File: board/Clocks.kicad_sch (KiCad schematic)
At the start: 9 parts, among them J4 ATX-20, U36 74HC14, U37 74LS191, Y1 14.31818MHz

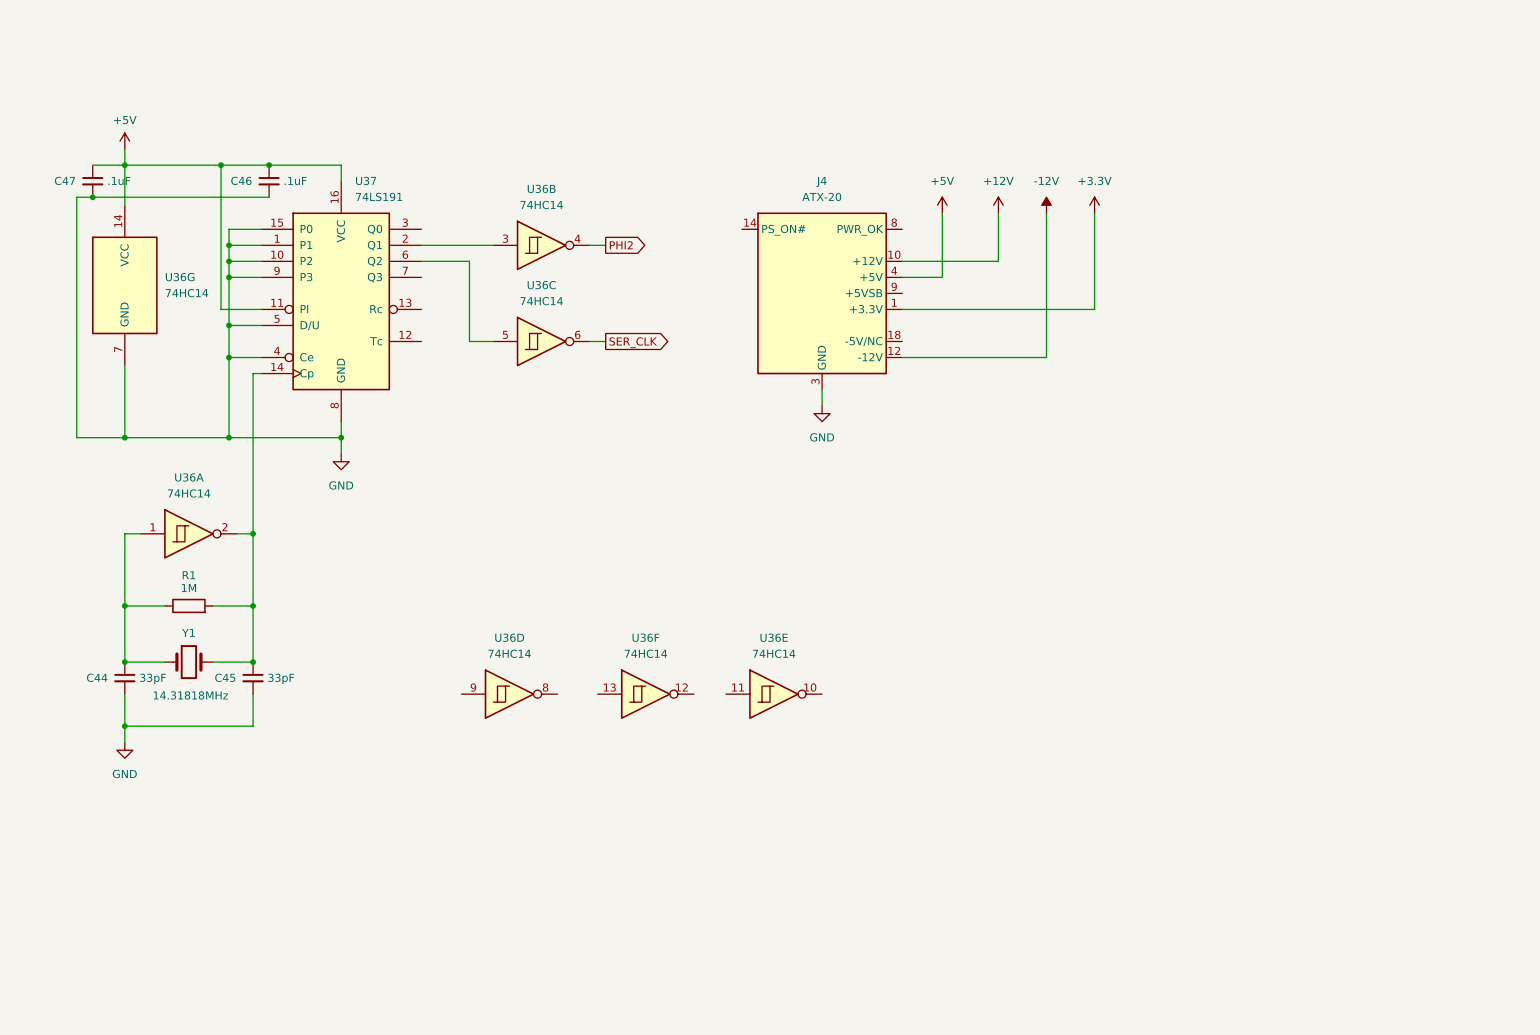
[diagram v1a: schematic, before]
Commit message: Changing to ATX-sized motherboard with 8 62-pin ISA slots.  Other component connection cleanup as well.
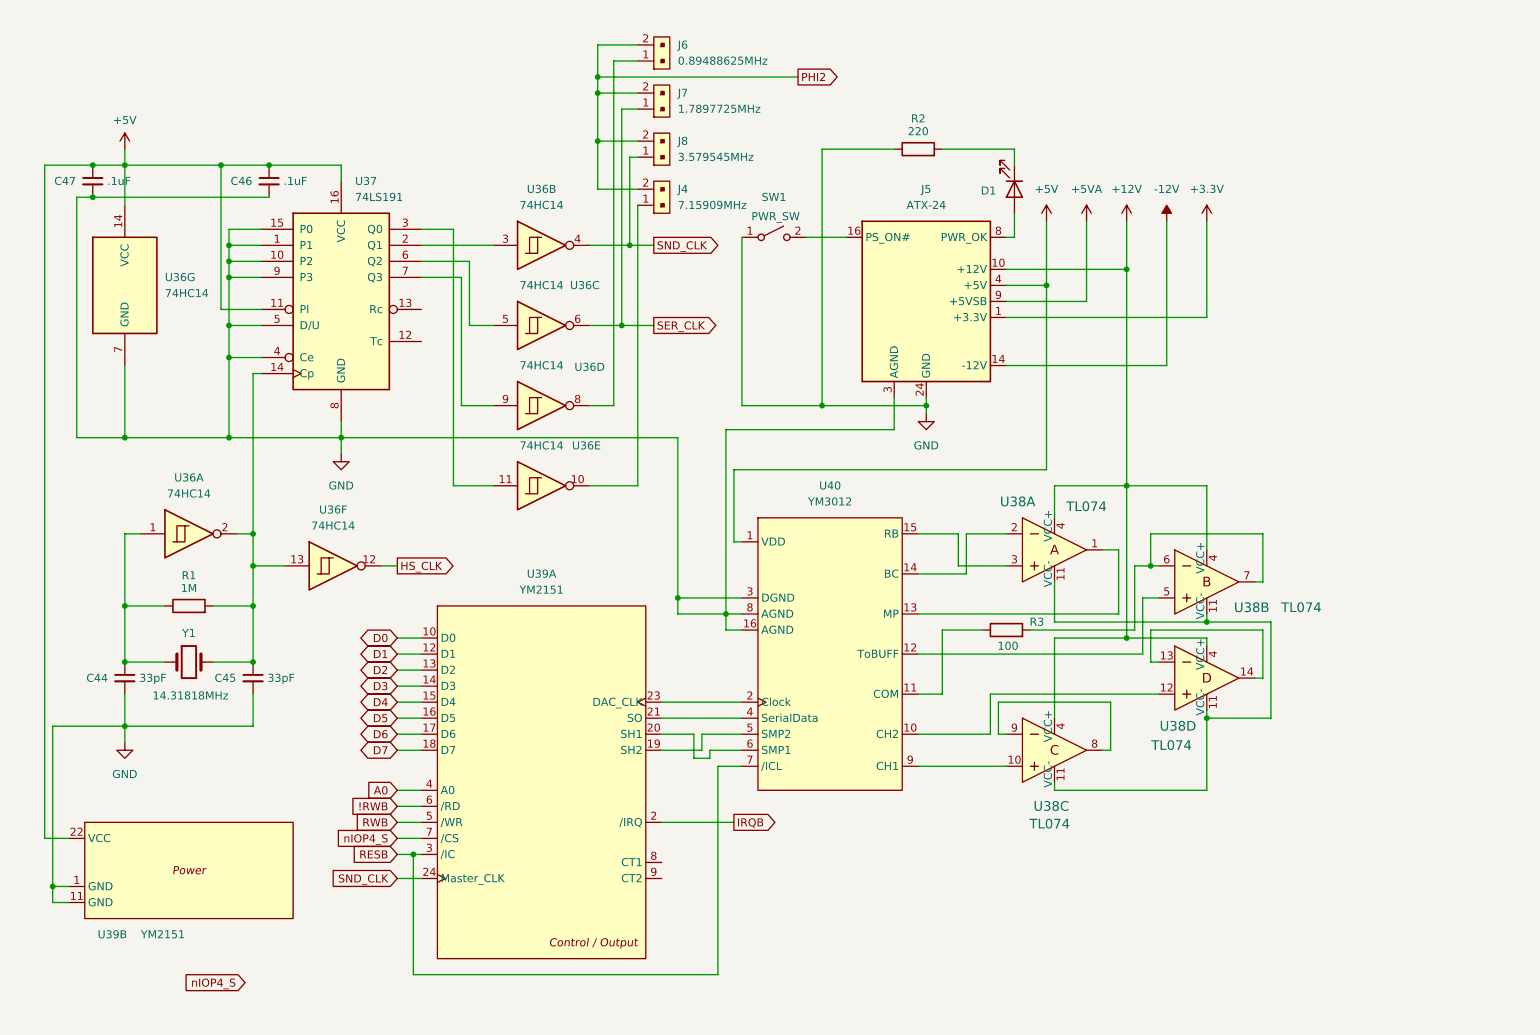
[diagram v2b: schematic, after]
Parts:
- removed J4: ATX-20, Connector_Molex:Molex_Mini-Fit_Jr_5566-20A_2x10_P4.20mm_Vertical, symbol Connector:ATX-20
- added D1: LED, LED_THT:LED_D3.0mm, symbol Device:LED
- added J4: 7.15909MHz, Connector_PinHeader_2.54mm:PinHeader_2x01_P2.54mm_Vertical, symbol dk_Rectangular-Connectors-Headers-Male-Pins:22-23-2021
- added J5: ATX-24, MolexATX24:CON_39299247, symbol Connector:ATX-24
- added J6: 0.89488625MHz, Connector_PinHeader_2.54mm:PinHeader_2x01_P2.54mm_Vertical, symbol dk_Rectangular-Connectors-Headers-Male-Pins:22-23-2021
- added J7: 1.7897725MHz, Connector_PinHeader_2.54mm:PinHeader_2x01_P2.54mm_Vertical, symbol dk_Rectangular-Connectors-Headers-Male-Pins:22-23-2021
- added J8: 3.579545MHz, Connector_PinHeader_2.54mm:PinHeader_2x01_P2.54mm_Vertical, symbol dk_Rectangular-Connectors-Headers-Male-Pins:22-23-2021
- added R2: 220, Resistor_THT:R_Axial_DIN0204_L3.6mm_D1.6mm_P5.08mm_Horizontal, symbol Device:R
- added R3: 100, Resistor_THT:R_Axial_DIN0204_L3.6mm_D1.6mm_P5.08mm_Horizontal, symbol Device:R
- added SW1: PWR_SW, Button_Switch_THT:SW_DIP_SPSTx01_Slide_6.7x4.1mm_W7.62mm_P2.54mm_LowProfile, symbol Switch:SW_SPST
- added U38: TL074, Package_DIP:DIP-14_W7.62mm_Socket_LongPads, symbol dk_Linear-Amplifiers-Instrumentation-OP-Amps-Buffer-Amps:TL074CN
- added U39: YM2151, Package_DIP:DIP-24_W15.24mm_Socket_LongPads, symbol Yamaha 2151-3012:YM2151
- added U40: YM3012, Package_DIP:DIP-16_W7.62mm_Socket_LongPads, symbol Yamaha 2151-3012:YM3012
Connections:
- net +12V: now also J5.10 (+12V), J5.11 (+12V), U38.4 (VCC+), U38.4 (VCC+), U38.4 (VCC+), U38.4 (VCC+)
- net +3.3V: now also J5.1 (+3.3V), J5.12 (+3.3V), J5.13 (+3.3V), J5.2 (+3.3V)
- net +5V: now also J5.21 (+5V), J5.22 (+5V), J5.23 (+5V), J5.4 (+5V), J5.6 (+5V), U39.22 (VCC), U40.1 (VDD)
- net -12V: now also J5.14 (-12V)
- net GND: now also J5.15 (GND), J5.17 (GND), J5.18 (GND), J5.19 (GND), J5.24 (GND), J5.3 (AGND), J5.5 (GND), J5.7 (GND), R2.1, SW1.1 (A), U39.1 (GND), U39.11 (GND), U40.16 (AGND), U40.3 (DGND), U40.8 (AGND)
- net PHI2: now also J4.2, J6.2, J7.2, J8.2; no longer U36.4
- net SER_CLK: now also J7.1
- net HS_CLK: now reaches U36.12
- net at U36.13: now also C45.1, R1.2, U36.2, U37.14 (Cp), Y1.2
- net at U37.3 (Q0): now also U36.11
- net at U37.7 (Q3): now also U36.9
- net at U36.10: now also J4.1
- net at U36.8: now also J6.1
- new net: U38.11 (VCC-), U38.11 (VCC-), U38.11 (VCC-), U38.11 (VCC-)
- new net: U38.12, U40.10 (CH2)
- new net: U38.13, U38.14
- new net: R3.1, U40.11 (COM)
- new net: R3.2, U38.6, U38.7
- new net: U38.1, U40.13 (MP)
- new net: U38.2, U40.14 (BC)
- new net: U38.3, U40.15 (RB)
- new net: J5.16 (PS_ON#), SW1.2 (B)
- new net: U38.5, U40.12 (ToBUFF)
- new net: U39.23 (DAC_CLK), U40.2 (Clock)
- new net: U39.21 (SO), U40.4 (SerialData)
- new net: U39.19 (SH2), U40.5 (SMP2)
- new net: U39.20 (SH1), U40.6 (SMP1)
- new net: U38.10, U40.9 (CH1)
- new net: D1.1 (K), R2.2
- new net: D1.2 (A), J5.8 (PWR_OK)
- new net: U38.8, U38.9
- new net !RWB: U39.6 (/RD)
- new net +5VA: J5.9 (+5VSB)
- new net A0: U39.4 (A0)
- new net D0: U39.10 (D0)
- new net D1: U39.12 (D1)
- new net D2: U39.13 (D2)
- new net D3: U39.14 (D3)
- new net D4: U39.15 (D4)
- new net D5: U39.16 (D5)
- new net D6: U39.17 (D6)
- new net D7: U39.18 (D7)
- new net IRQB: U39.2 (/IRQ)
- new net RESB: U39.3 (/IC), U40.7 (/ICL)
- new net RWB: U39.5 (/WR)
- new net SND_CLK: J8.1, U36.4, U39.24 (Master_CLK)
- new net nIOP4_S: U39.7 (/CS)
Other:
- moved on the sheet: U36C, U36D, U36E, U36F

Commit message: Added surface mount version of memory daughter cards, and lots of schematic updates and fixes, including adding dedicated registers for shared memory bank select at $FFF1 and IRQ vTable entry selector at $FFF2 along with the IRQ vTable registers and priority encoders for 16 IRQs
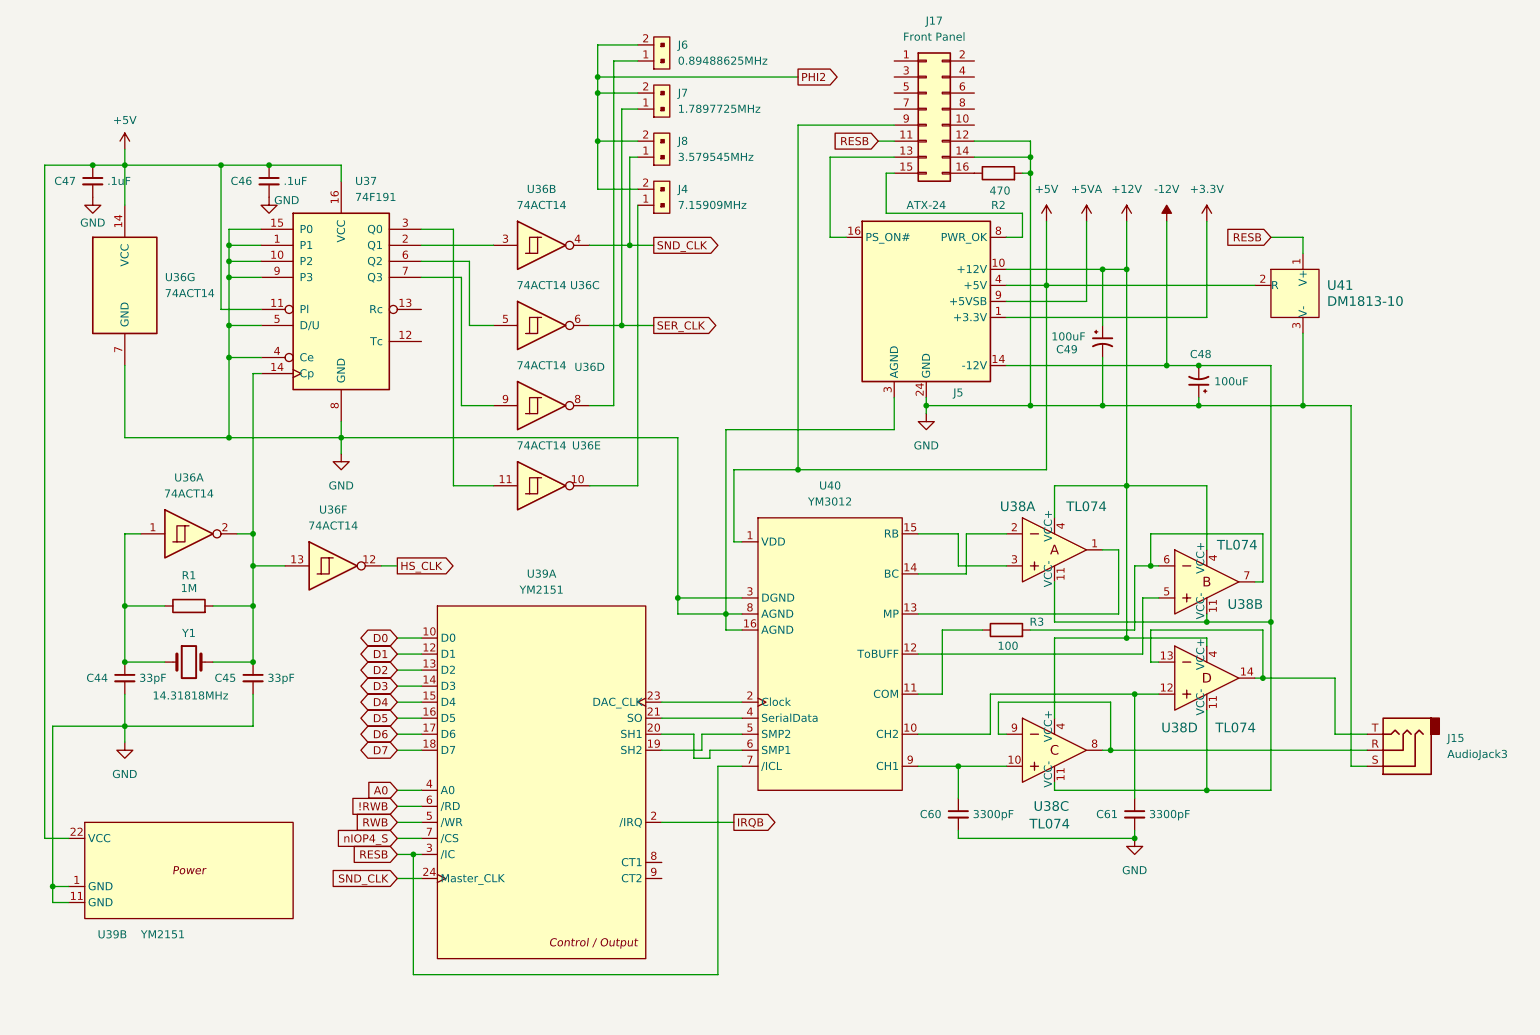
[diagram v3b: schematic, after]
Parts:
- removed D1: LED, LED_THT:LED_D3.0mm, symbol Device:LED
- removed SW1: PWR_SW, Button_Switch_THT:SW_DIP_SPSTx01_Slide_6.7x4.1mm_W7.62mm_P2.54mm_LowProfile, symbol Switch:SW_SPST
- added C48, C49: 100uF, Capacitor_THT:CP_Radial_D5.0mm_P2.50mm, symbol Device:C_Polarized_Small_US
- added C60, C61: 3300pF, Capacitor_THT:C_Disc_D5.0mm_W2.5mm_P2.50mm, symbol Device:C_Small
- added J15: AudioJack3, Connector_Audio:Jack_3.5mm_CUI_SJ1-3523N_Horizontal, symbol Connector_Audio:AudioJack3
- added J17: Front Panel, Connector_PinHeader_2.54mm:PinHeader_2x08_P2.54mm_Vertical, symbol Connector_Generic:Conn_02x08_Odd_Even
- added U41: DM1813-10, Package_TO_SOT_THT:TO-92L_Inline_Wide, symbol dk_PMIC-Current-Regulation-Management:LM334Z_NOPB
- R2: value 220 -> 470
- U36: value 74HC14 -> 74ACT14
- U37: value 74LS191 -> 74F191
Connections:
- net +12V: now also C49.1
- net +5V: now also J17.9 (Pin_9), U41.2 (R)
- net -12V: now also U38.11 (VCC-), U38.11 (VCC-), U38.11 (VCC-), U38.11 (VCC-), C48.2
- net GND: now also R2.2, C48.1, C49.2, C60.2, C61.2, J15.S, J17.12 (Pin_12), J17.14 (Pin_14), U41.3 (V-); no longer R2.1
- net RESB: now also J17.11 (Pin_11), U41.1 (V+)
- net at U38.12, U40.10 (CH2): now also C61.1
- net at U38.13, U38.14: now also J15.T
- net at J5.16 (PS_ON#): now also J17.13 (Pin_13)
- net at U38.10, U40.9 (CH1): now also C60.1
- net at J5.8 (PWR_OK): now also J17.15 (Pin_15)
- net at U38.8, U38.9: now also J15.R
- new net: J17.16 (Pin_16), R2.1

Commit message: More main PCB updates.  Rearranged some things.  Bypass caps near PS connector.  Moved front panel connector to opposite side of board.
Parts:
- added C67, C68, C69: 100uF, Capacitor_THT:CP_Radial_D5.0mm_P2.50mm, symbol Device:C_Polarized_Small_US
- J15: footprint Connector_Audio:Jack_3.5mm_CUI_SJ1-3523N_Horizontal -> Connector_Audio:Jack_3.5mm_CUI_SJ1-3524N_Horizontal
- U38: footprint Package_DIP:DIP-14_W7.62mm_Socket_LongPads -> Package_DIP:DIP-16_W7.62mm_Socket_LongPads
- U39: footprint Package_DIP:DIP-24_W15.24mm_Socket_LongPads -> Package_DIP:DIP-24_W15.24mm
- U41: footprint Package_TO_SOT_THT:TO-92L_Inline_Wide -> Package_TO_SOT_THT:TO-92_Inline_Wide; DK_Datasheet_Link (none) -> http://www.ti.com/general/docs/suppproductinfo.tsp?distId=1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; DK_Detail_Page (none) -> /product-detail/en/texas-instruments/LM334Z-NOPB/LM334ZNS-N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; Description_1 AnalogDevices DM1813 Reset Monitor -> IC CURRENT SOURCE 3% TO92-3; Digi-Key_PN (none) -> LM334ZNS/NOPB-ND; Family P -> PMIC - Current Regulation/Management; MPN (none) -> LM334Z/NOPB; Manufacturer AnalogDevices -> Texas Instruments
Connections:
- net +3.3V: now also C69.1
- net +5V: now also C67.1
- net +5VA: now also C68.1
- net GND: now also C67.2, C68.2, C69.2
- net IRQB renamed nIRQ4

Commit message: Latest main PCB update with FFF1 and FFF2 added and decode logic updated to exclude FFFE and FFFF in nOSROM_S signal
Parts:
- U36: footprint Package_DIP:DIP-14_W7.62mm_LongPads -> Package_DIP:DIP-14_W7.62mm_Socket_LongPads
- U37: footprint Package_DIP:DIP-16_W7.62mm_LongPads -> Package_DIP:DIP-16_W7.62mm_Socket_LongPads
- U39: footprint Package_DIP:DIP-24_W15.24mm -> Package_DIP:DIP-24_W15.24mm_Socket_LongPads
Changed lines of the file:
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@@
 			)
 		)
-		(property "Footprint" "Package_DIP:DIP-14_W7.62mm_LongPads"
+		(property "Footprint" "Package_DIP:DIP-14_W7.62mm_Socket_LongPads"
 			(at 78.74 101.6 0)
 			(effects
@@
 			)
 		)
-		(property "Footprint" "Package_DIP:DIP-16_W7.62mm_LongPads"
+		(property "Footprint" "Package_DIP:DIP-16_W7.62mm_Socket_LongPads"
 			(at 80.01 58.42 0)
 			(effects
@@
 			)
 		)
-		(property "Footprint" "Package_DIP:DIP-14_W7.62mm_LongPads"
+		(property "Footprint" "Package_DIP:DIP-14_W7.62mm_Socket_LongPads"
 			(at 111.76 63.5 0)
 			(effects
@@
 			)
 		)
-		(property "Footprint" "Package_DIP:DIP-14_W7.62mm_LongPads"
+		(property "Footprint" "Package_DIP:DIP-14_W7.62mm_Socket_LongPads"
 			(at 111.76 88.9 0)
 			(effects
@@
 			)
 		)
-		(property "Footprint" "Package_DIP:DIP-14_W7.62mm_LongPads"
+		(property "Footprint" "Package_DIP:DIP-14_W7.62mm_Socket_LongPads"
 			(at 111.76 76.2 0)
 			(effects
@@
 			)
 		)
-		(property "Footprint" "Package_DIP:DIP-14_W7.62mm_LongPads"
+		(property "Footprint" "Package_DIP:DIP-14_W7.62mm_Socket_LongPads"
 			(at 111.76 50.8 0)
 			(effects
@@
 			)
 		)
-		(property "Footprint" "Package_DIP:DIP-14_W7.62mm_LongPads"
+		(property "Footprint" "Package_DIP:DIP-14_W7.62mm_Socket_LongPads"
 			(at 55.88 96.52 0)
 			(effects
@@
 			)
 		)
-		(property "Footprint" "Package_DIP:DIP-24_W15.24mm"
+		(property "Footprint" "Package_DIP:DIP-24_W15.24mm_Socket_LongPads"
 			(at 92.71 161.29 0)
 			(effects
@@
 			)
 		)
-		(property "Footprint" "Package_DIP:DIP-24_W15.24mm"
+		(property "Footprint" "Package_DIP:DIP-24_W15.24mm_Socket_LongPads"
 			(at 36.83 195.58 0)
 			(effects
@@
 			)
 		)
-		(property "Footprint" "Package_DIP:DIP-14_W7.62mm_LongPads"
+		(property "Footprint" "Package_DIP:DIP-14_W7.62mm_Socket_LongPads"
 			(at 45.72 57.15 0)
 			(effects

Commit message: Updated schematics with larger mounting holes (4mm vs 3.2mm) and larger electrolytic cap footprints
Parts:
- C48, C49, C67, C68, C69: footprint Capacitor_THT:CP_Radial_D5.0mm_P2.50mm -> Capacitor_THT:CP_Radial_D6.3mm_P2.50mm
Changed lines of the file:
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@@
 			)
 		)
-		(property "Footprint" "Capacitor_THT:CP_Radial_D5.0mm_P2.50mm"
+		(property "Footprint" "Capacitor_THT:CP_Radial_D6.3mm_P2.50mm"
 			(at 207.01 73.66 0)
 			(effects
@@
 			)
 		)
-		(property "Footprint" "Capacitor_THT:CP_Radial_D5.0mm_P2.50mm"
+		(property "Footprint" "Capacitor_THT:CP_Radial_D6.3mm_P2.50mm"
 			(at 224.79 73.66 0)
 			(effects
@@
 			)
 		)
-		(property "Footprint" "Capacitor_THT:CP_Radial_D5.0mm_P2.50mm"
+		(property "Footprint" "Capacitor_THT:CP_Radial_D6.3mm_P2.50mm"
 			(at 194.31 73.66 0)
 			(effects
@@
 			)
 		)
-		(property "Footprint" "Capacitor_THT:CP_Radial_D5.0mm_P2.50mm"
+		(property "Footprint" "Capacitor_THT:CP_Radial_D6.3mm_P2.50mm"
 			(at 200.66 66.04 0)
 			(effects
@@
 			)
 		)
-		(property "Footprint" "Capacitor_THT:CP_Radial_D5.0mm_P2.50mm"
+		(property "Footprint" "Capacitor_THT:CP_Radial_D6.3mm_P2.50mm"
 			(at 215.9 72.39 0)
 			(effects
